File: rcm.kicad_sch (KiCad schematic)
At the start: 150 parts, among them Y1 8MHz, Y2 32.768kHz

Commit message: rcm: drop the ESP32 add-on, and fix three more issues found pre-PCB
ESP32-C3 co-processor dropped per the user; PA9/PA10 become ordinary spares.

Second review pass against datasheets found three more problems that ERC and the
netlist round-trip both passed:

- No I2C pull-ups anywhere. The BMI270 would never have responded. The datasheet
  line about not needing external pull-ups applies to the auxiliary interface,
  not the primary. 4.7k added; revB already had these as R9/R10.
- The sense divider failed VIH at rest voltage. 74HC VIH(min) is 0.7*Vcc = 2.31V
  at 3V3, not the ~1.65V typical switching point, so 1M/220k gave 2.16V at 12.0V
  and every channel would have read "circuit broken" with the engine off.
  Corrected to 1M/270k: 2.55V at 12.0V, still under 3V3 at charging voltage so
  the input protection diodes never conduct.
- BOOT0 was pulled down with no jumper, leaving USB DFU unreachable. Added
  J_BOOT, and an R_ADDR_ALT DNP jumper for the IMU 0x69 address, both mirroring
  revB's pattern.

Checked revB for the IMU faults found here: it is CORRECT on both counts - CSB
goes to +3V3, and R57 (fitted) pulls SDO low for 0x68 with R58 (DNP) as the
alternate. The earlier concern about a floating SDO was wrong; I had queried R58
and missed its partner R57.

154 components, ERC 0, netlist round-trip MATCH.

Co-Authored-By: Claude Opus 5 <noreply@anthropic.com>
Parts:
- added J_BOOT: BOOT_SEL, Connector_PinHeader_2.54mm:PinHeader_1x03_P2.54mm_Vertical, symbol Connector_Generic:Conn_01x03
- added R_ADDR_ALT: 0R, Resistor_SMD:R_0805_2012Metric, symbol Device:R
- added R_SCL, R_SDA: 4.7k, Resistor_SMD:R_0805_2012Metric, symbol Device:R
- R_AL1, R_AL2, R_AL3, R_IGL, R_SL1, R_SL10, R_SL11, R_SL12, R_SL13, R_SL14, R_SL15, R_SL16, R_SL17, R_SL18, R_SL19, R_SL2, R_SL20, R_SL21, R_SL3, R_SL4, R_SL5, R_SL6, R_SL7, R_SL8, R_SL9: value 220k -> 270k
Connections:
- net +3V3: now also J_BOOT.1 (Pin_1), R_ADDR_ALT.2, R_SCL.1, R_SDA.1
- net BOOT0: now also J_BOOT.2 (Pin_2)
- net GND: now also J_BOOT.3 (Pin_3)
- net IMU_SCL: now also R_SCL.2
- net IMU_SDA: now also R_SDA.2
- net IMU_SDO: now also R_ADDR_ALT.1

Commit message: rcm: board placement complete - 100x100mm, lint clean, DRC 0 errors
All 154 parts positioned. The three channel tiles are defined once as a
27-member group and instantiated three times, so 81 of the 154 placements come
from a single definition - the payoff for choosing the shift-register layout.

Board is 100x100mm against revB's 216x148, roughly a quarter the area.

The trap worth recording: JB1 and JB2 are separate footprints for the two
columns of one buck module, and their courtyards never touch, so nothing checks
that they line up. They must be 27.80mm apart in X and offset 1.90mm in Y,
because the IN column's first hole sits 3.60mm from the module edge and the OUT
column's sits 1.70mm. They were first placed level, which would have meant the
module did not fit at all. The module body also has no courtyard by design, so
gen_plan.py now asserts nothing is placed underneath it.

Placement lint 0/0; board DRC 0 errors. The 53 remaining warnings are all
silkscreen and get cleaned up in the dedicated pass at the end. 414 unconnected
items are expected - routing is the next step.

Co-Authored-By: Claude Opus 5 <noreply@anthropic.com>
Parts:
- J_USB: footprint Connector_USB:USB_C_Receptacle_USB2.0_16P -> Connector_USB:USB_C_Receptacle_HCTL_HC-TYPE-C-16P-01A

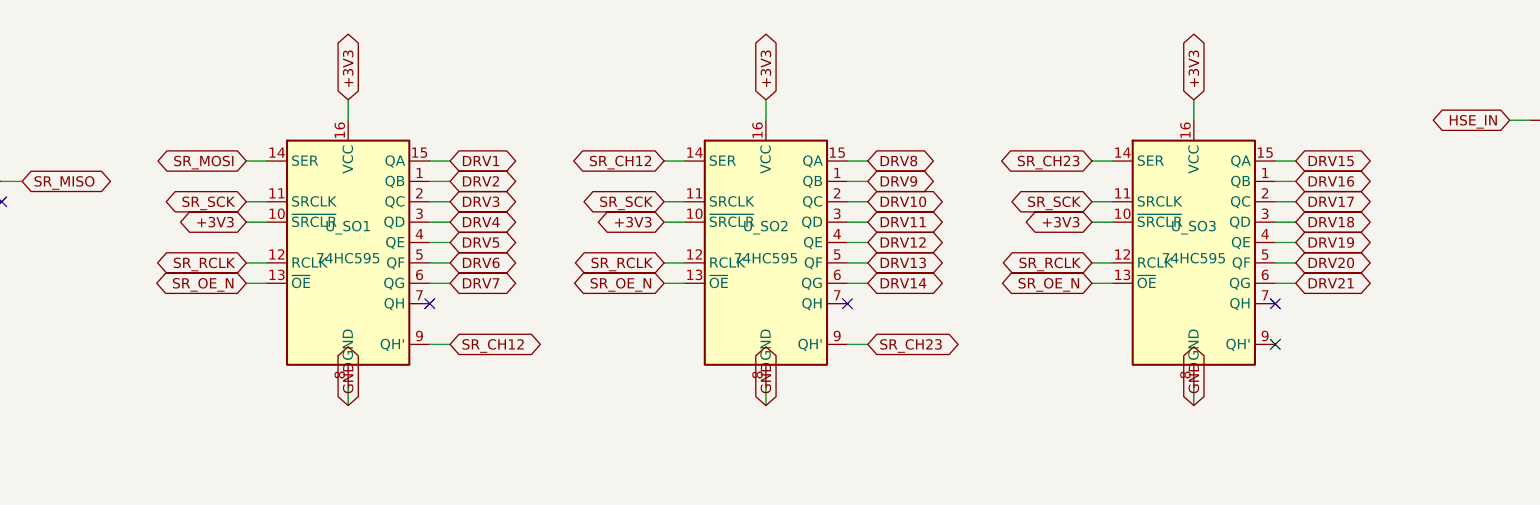
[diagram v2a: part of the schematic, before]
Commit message: rcm: reverse the 595 data chain and give the mounting holes washer clearance
Reviewing the rendered board, the shift-register data line entered at the tile
FURTHEST from the MCU - a ~74mm haul across the board before the chain doubled
back east past the MCU. Reversed so it enters at the nearest tile and ripples
away. Sets the bit order: first byte out lands in U_SO1 (channels 1-7).

The four mounting holes all sat 3.5-4.0mm from a board edge, which is exactly
the radius of an M3 washer - it would have overhung. Moved to 5mm+ and lifted
the two bottom holes clear of the terminal-block row.

Schematic ERC 0 and round-trip MATCH; placement lint 0/0; board DRC 0 errors.

Co-Authored-By: Claude Opus 5 <noreply@anthropic.com>
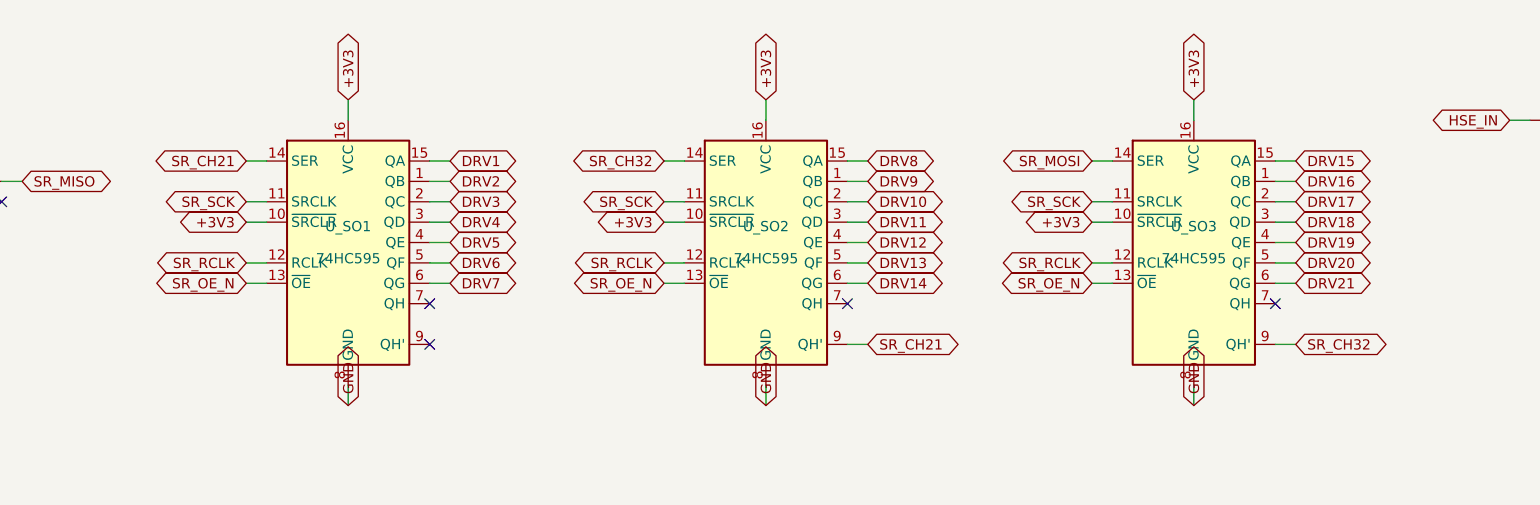
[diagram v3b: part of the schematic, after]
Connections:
- net SR_MOSI: now also U_SO3.14 (SER); no longer U_SO1.14 (SER)
- net SR_CH32: now reaches U_SO3.9 (QH')
- net SR_CH32: now also U_SO2.14 (SER)
- net SR_CH12: no longer names the net of U_SO1.9 (QH')
- net SR_CH12: no longer U_SO2.14 (SER)
- net SR_CH23 renamed SR_CH21
- net SR_CH21: now also U_SO1.14 (SER); no longer U_SO3.14 (SER)

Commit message: rcm: shift the MCU into the dead space, and fix the button pull-up for wetting current
MCU moved right and down into the empty area, away from the tight strip above it.
The decoupling row and R_BOOT are now positioned relative to the MCU so the BOOT0
escape lane fixed last round travels with it. Round 6 routes 414/414 with 0
unconnected and 0 DRC errors, in 2149 segments - fewer than before, so the move
improved routability slightly.

Button pull-up 100k -> 10k. At 12V a 100k pull-up passes only ~120uA through a
closed contact, below the ~1mA most mechanical contacts need to break through
surface film. Gold contacts are fine at microamps, ordinary automotive buttons
are not, and it fails in the worst way: perfect on the bench, intermittent months
later in a damp vibrating car. 10k gives 1.2mA on press and does not move the
logic levels. Patched into the placed board in-place rather than regenerating,
which would have wiped the routing.

Recorded the answer on momentary buttons: they work, and they beat a mechanical
latching switch because a latched switch can be physically stuck in the wrong
position when something else changes the state, whereas a momentary button has
no position to be wrong about. Also noted debouncing is mandatory and that each
button costs two channels.

Co-Authored-By: Claude Opus 5 <noreply@anthropic.com>
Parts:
- R_PU1, R_PU10, R_PU11, R_PU12, R_PU13, R_PU14, R_PU15, R_PU16, R_PU17, R_PU18, R_PU19, R_PU2, R_PU20, R_PU21, R_PU3, R_PU4, R_PU5, R_PU6, R_PU7, R_PU8, R_PU9: value 100k -> 10k

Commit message: rcm: resistor rows re-ordered, BOM sourced, manufacturing files out
Placement (user request): the three southern resistor rows keep their
6.0/10.5/15.0mm centre spacing, but R_PU moves to the southern row and
R_SH to the middle, both at rotation 0, with R_SL to the north row at
180. Laying them flat cleared nearly all the silkscreen crowding in the
south tiles.

BOM sourcing is complete - every line that gets assembled now has an
LCSC number. Four substitutions came out of it and are folded back into
gen_spec.py so the schematic agrees rather than the choice living only
in a side file:

  - AMS1117-3.3 for LD1117S33: JLC basic part, and pin-identical by
    construction (both symbols extend AP1117-15).
  - M95640 for 25LC640: $0.33 against $0.73-1.42 and better stocked,
    same 25-series SPI pinout the generic symbol already describes.
  - 60V PPTC over 30V: the SMAJ33A clamps near 53V.
  - 20pF for 12pF crystal load caps. This one was a genuine error, not
    a cost change: the 12.5pF crystal wants ~19pF, and 12pF ran the RTC
    about 22ppm fast - a minute a month. Also deletes a BOM line.

jlc_parts.json is rekeyed to 'value|footprint', which is what the BOM
script actually looks up; keyed by bare value it silently matched
nothing and would have produced an entirely unsourced BOM. The
footprint half earned its keep immediately by catching that the cheap
basic 8MHz crystal is HC-49S-SMD and would not fit the 5032 lands.
gen_spec.py now stamps an LCSC field onto every symbol from that same
file, and fails the build if a component has no line.

Two new shared tools: shrink_refs.py (0.8mm ref text on crowded parts,
which is what lets relocate_refs converge) and fix_marginal_clearance.py
(narrow rather than move segments that miss a rule by microns).

Board: 414/414 routed, 0 unconnected, 0 schematic parity. One clearance
violation survives at 1.3 microns short - deterministic, understood, and
documented in SPEC.md along with the three rejected fixes.

Gerbers export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
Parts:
- removed U_LDO: LD1117S33, Package_TO_SOT_SMD:SOT-223-3_TabPin2, symbol Regulator_Linear:LD1117S33TR_SOT223
- added U_LDO: AMS1117-3.3, Package_TO_SOT_SMD:SOT-223-3_TabPin2, symbol Regulator_Linear:AMS1117-3.3
- C_3V3I, C_5V: LCSC (none) -> C15850
- C_3V3O, C_CAN, C_EEP, C_IMU1, C_IMU2, C_LSW, C_LVS, C_M1, C_M2, C_M3, C_M4, C_M5, C_NRST, C_SI1, C_SI2, C_SI3, C_SO1, C_SO2, C_SO3, C_VDDA: LCSC (none) -> C49678
- C_BULK: LCSC (none) -> C2918502
- C_MB: LCSC (none) -> C1779
- C_VCAP: LCSC (none) -> C77081
- C_Y1A, C_Y1B: LCSC (none) -> C1798
- C_Y2A, C_Y2B: value 12pF -> 20pF; LCSC (none) -> C1798
- D1: LCSC (none) -> C8678
- D2: LCSC (none) -> C353454
- D_CAN: LCSC (none) -> C233494
- D_LED1: LCSC (none) -> C84260
- D_LED2: LCSC (none) -> C84256
- F1: LCSC (none) -> C19078719
- J_AUX, J_CAN1, J_CAN2: LCSC (none) -> C441322
- J_CH1, J_CH2, J_CH3: LCSC (none) -> C441326
- J_IGN, J_PWR: LCSC (none) -> C441321
- J_USB: LCSC (none) -> C165948
- R_ADDR, R_ADDR_ALT, R_TJ: LCSC (none) -> C17477
- R_AH1, R_AH2, R_AH3, R_IGH, R_SH1, R_SH10, R_SH11, R_SH12, R_SH13, R_SH14, R_SH15, R_SH16, R_SH17, R_SH18, R_SH19, R_SH2, R_SH20, R_SH21, R_SH3, R_SH4, R_SH5, R_SH6, R_SH7, R_SH8, R_SH9: LCSC (none) -> C17514
- R_AL1, R_AL2, R_AL3, R_IGL, R_SL1, R_SL10, R_SL11, R_SL12, R_SL13, R_SL14, R_SL15, R_SL16, R_SL17, R_SL18, R_SL19, R_SL2, R_SL20, R_SL21, R_SL3, R_SL4, R_SL5, R_SL6, R_SL7, R_SL8, R_SL9: LCSC (none) -> C17589
- R_BOOT, R_OE, R_PU1, R_PU10, R_PU11, R_PU12, R_PU13, R_PU14, R_PU15, R_PU16, R_PU17, R_PU18, R_PU19, R_PU2, R_PU20, R_PU21, R_PU3, R_PU4, R_PU5, R_PU6, R_PU7, R_PU8, R_PU9, R_RS: LCSC (none) -> C17414
- R_CC1, R_CC2: LCSC (none) -> C27834
- R_LED1, R_LED2, R_LHOLD: LCSC (none) -> C17513
- R_LG: LCSC (none) -> C17714
- R_LIGN: LCSC (none) -> C17713
- R_LPD: LCSC (none) -> C17560
- R_SCL, R_SDA: LCSC (none) -> C17673
- R_TERM: LCSC (none) -> C17437
- SW_RST: LCSC (none) -> C2886894
- U_CAN: LCSC (none) -> C12084
- U_DRV1, U_DRV2, U_DRV3: LCSC (none) -> C2149827
- U_EEP: value 25LC640 -> M95640; LCSC (none) -> C283461
- U_IMU: LCSC (none) -> C2836813
- U_LATCH: LCSC (none) -> C534837
- U_MCU: LCSC (none) -> C69336
- U_SI1, U_SI2, U_SI3: LCSC (none) -> C22384789
- U_SO1, U_SO2, U_SO3: LCSC (none) -> C5947
- Y1: LCSC (none) -> C115962
- Y2: LCSC (none) -> C32346
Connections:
- net +3V3: now also U_LDO.2 (VO)
- net +5V: now also U_LDO.3 (VI)
- net GND: now also U_LDO.1 (GND)

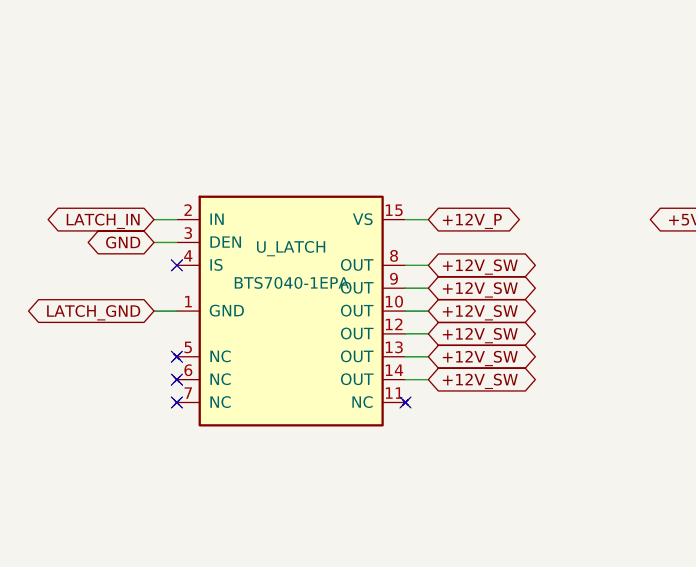
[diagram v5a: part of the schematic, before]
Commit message: rcm: latch part -> BTS7040-1EPZ, C534837 went to zero stock
JLC's quote priced 38 of 39 BOM lines; C534837 (BTS7040-1EPA) is
unbuyable. Swapped to C534838, BTS7040-1EPZ: same base part number, so
the Z is a temperature/variant grade rather than a different die and the
pinout is near-certain rather than resting on family convention. Same
PG-TSDSO-14-22 package, and better on both specs that matter - 19mOhm
against 36, and -40..+175C against +150.

The RCM:BTS70xx-1E symbol was built as a generic family part, which is
what made this a value-string change rather than a re-layout.

Stock is thin at ~10 pieces - enough for this run of 5 with spares. If it
goes, fall back to C534825 BTS7004-1EPP (~20k stock, overkill at
4.4mOhm/15A but harmless, same package and family pinout), which would
want a datasheet pinout check since it is not the same base part.

Rebuilt and re-routed WITH --zone GND:F.Cu --zone GND:B.Cu this time.
414/414 routed, 0 unconnected, 0 schematic parity, 2 filled GND pours,
and five pads set solid where thermal spokes came up short.

The 1.3 micron clearance miss is gone - this route avoids it - so the
board is now clean of every non-silkscreen violation, leaving 26 cosmetic
silkscreen warnings. That also corrects the earlier reading of it as
deterministic geometry: it was route-dependent, just not across the
routes tried at the time.

Gerbers, BOM and CPL regenerated.

Co-Authored-By: Claude Opus 5 <noreply@anthropic.com>
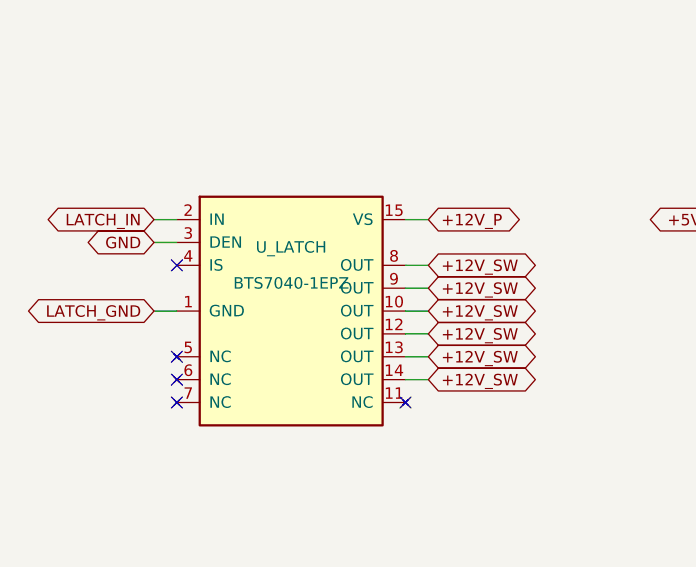
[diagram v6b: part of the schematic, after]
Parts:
- U_LATCH: value BTS7040-1EPA -> BTS7040-1EPZ; LCSC C534837 -> C534838

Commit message: rcm: channel mode becomes a software table; add config DIP switch
Abandons the 21-DIP-switch plan and makes the board simpler instead.

The blocker was only ever the pull-UP: R_PU as 10k to +12V makes a blown
fuse read 2.531V and a good one 2.551V - both HIGH, 20mV apart, fuse
sensing dead. A 10k pull-DOWN does not, because the ~85 ohm relay coil
swamps it. All four states then read correctly with the SAME resistor
fitted on every channel:

  output, fuse good   2.530V HIGH      input, button open    0.000V LOW
  output, fuse blown  0.000V LOW       input, button closed  2.551V HIGH

So nothing is mode-dependent, there is nothing for hardware to select,
and in/out is purely a firmware table. R_PU is now fitted 10k to GND on
all 21 channels. That deleted the DIP array, the readback, the P-FET
rails and the south-half re-layout in one go.

Trade: buttons are positive-switched to +12V. Wetting current goes to
1.20mA (against 0.0094mA on the divider alone), and a chafed button wire
now reads 'not pressed' rather than phantom-activating.

Adds SW_CFG, one 8-way 1.27mm DIP in the top-right corner - the only free
10x10mm pocket, and next to J_CAN2 where the termination pole must reach.
Pos 1 CAN termination (passive, parallels R_TJ); pos 2-6 role, address
x2, bitrate, IMU publish enable, on PC0-PC4 using the STM32's internal
pull-ups so no external resistors are needed. These are the settings that
cannot be fixed over the bus once wrong.

Positions 7-8 are left unconnected deliberately: routing two more nets
from that corner across the CAN/IMU corridor is what tipped the board
from routable to not (3 nets failed, then 1). Dropping them fixed it.

426/426 routed, 0 unconnected, 0 schematic parity, 2 filled GND pours,
25 cosmetic silkscreen warnings and no electrical violations at all.
BOM 40 lines all sourced, CPL 149 placements.

VERIFY the DIP land before ordering - standard 1.27mm 8-position
gull-wing footprint, part not checked against a drawing.

Co-Authored-By: Claude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
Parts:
- added SW_CFG: CFG_DIP, Button_Switch_SMD:SW_DIP_SPSTx08_Slide_KingTek_DSHP08TS_W7.62mm_P1.27mm, symbol Switch:SW_DIP_x08
- R_PU1, R_PU10, R_PU11, R_PU12, R_PU13, R_PU14, R_PU15, R_PU16, R_PU17, R_PU18, R_PU19, R_PU2, R_PU20, R_PU21, R_PU3, R_PU4, R_PU5, R_PU6, R_PU7, R_PU8, R_PU9: now fitted
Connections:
- net +12V_P: no longer R_PU1.2, R_PU10.2, R_PU11.2, R_PU12.2, R_PU13.2, R_PU14.2, R_PU15.2, R_PU16.2, R_PU17.2, R_PU18.2, R_PU19.2, R_PU2.2, R_PU20.2, R_PU21.2, R_PU3.2, R_PU4.2, R_PU5.2, R_PU6.2, R_PU7.2, R_PU8.2, R_PU9.2
- net CANL: now also SW_CFG.16
- net CAN_TERM: now also SW_CFG.1
- net GND: now also R_PU1.2, R_PU10.2, R_PU11.2, R_PU12.2, R_PU13.2, R_PU14.2, R_PU15.2, R_PU16.2, R_PU17.2, R_PU18.2, R_PU19.2, R_PU2.2, R_PU20.2, R_PU21.2, R_PU3.2, R_PU4.2, R_PU5.2, R_PU6.2, R_PU7.2, R_PU8.2, R_PU9.2, SW_CFG.11, SW_CFG.12, SW_CFG.13, SW_CFG.14, SW_CFG.15
- net CFG_ADDR1: now reaches U_MCU.10 (PC2)
- net CFG_ADDR1: now also SW_CFG.4
- net CFG_BAUD: now reaches U_MCU.11 (PC3)
- net CFG_BAUD: now also SW_CFG.5
- net CFG_IMU_EN: now reaches U_MCU.24 (PC4)
- net CFG_IMU_EN: now also SW_CFG.6
- net CFG_ROLE: now reaches U_MCU.8 (PC0)
- net CFG_ROLE: now also SW_CFG.2
- net CFG_ADDR0: now reaches U_MCU.9 (PC1)
- net CFG_ADDR0: now also SW_CFG.3
- no-connect marks 43 -> 42

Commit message: rcm: C_VCAP -> C377773, the only Basic swap available in the BOM
Checked all 20 Extended lines in the JLC assembly order against the Basic
library. Exactly one has a Basic equivalent:

  C_VCAP  2.2uF 0805  C77081 (ext) -> C377773 (BASIC), 1.7M stock

50V/X5R against 25V/X7R: voltage is irrelevant at ~1.2V on VCAP and there
is no DC bias derating worth mentioning, but X5R tops out at +85C where
X7R reaches +125C. Fine for a cabin-mounted board; worth knowing if it
ever moves somewhere hot.

Nothing else converts. The remaining 19 Extended lines are specialist ICs
(MCU, IMU, CAN transceiver, TPL7407L, EEPROM, PROFET, 74HC165),
connectors (three terminal sizes, USB-C, DIP switch) and a handful of
parts with genuinely no Basic equivalent at JLC - 270k 0805, 10uF 50V
1210, SMAJ33A, the PPTC, the green LED. JLC's Basic library is nearly all
common passives, and this BOM's passives were already Basic.

Both mfg/ and mfg4/ BOMs regenerated; schematic stamped and ERC-clean.

Co-Authored-By: Claude Opus 5 <noreply@anthropic.com>
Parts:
- C_VCAP: LCSC C77081 -> C377773
